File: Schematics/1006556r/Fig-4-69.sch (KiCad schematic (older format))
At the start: 0 parts

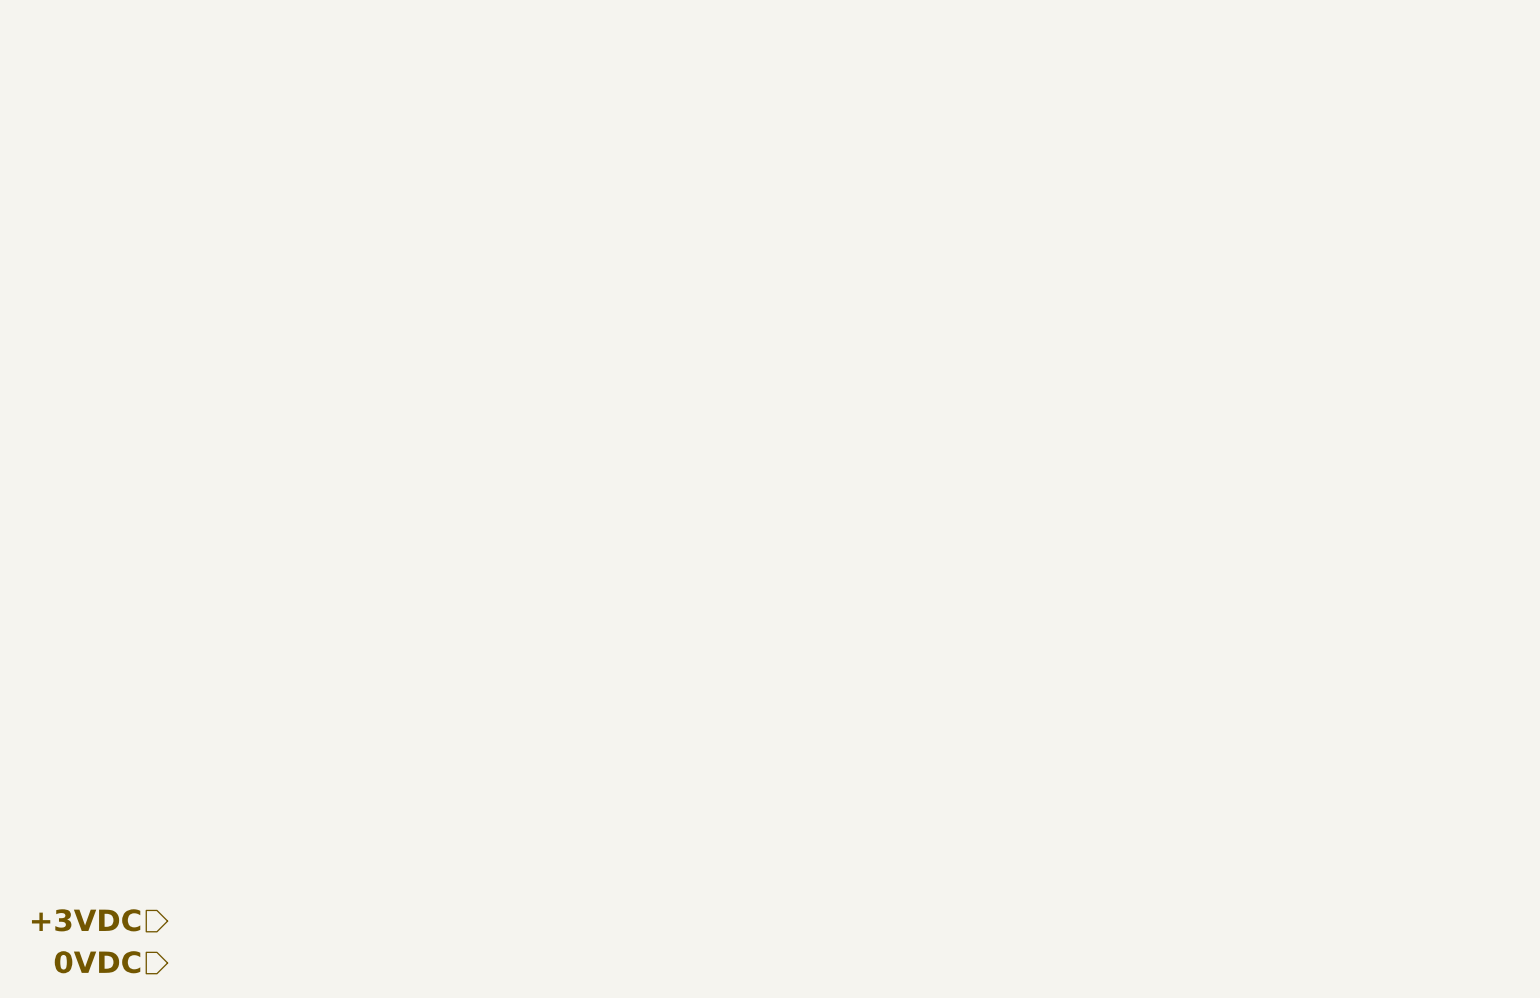
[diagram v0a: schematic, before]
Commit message: For module A31, transcribed through Fig 4-87, leaving just 88, 91, 93, 114, 141, and 147 to go, plus their integration into the top-level sheet (and resolution of remaining inconsistencies in ND-1021041).
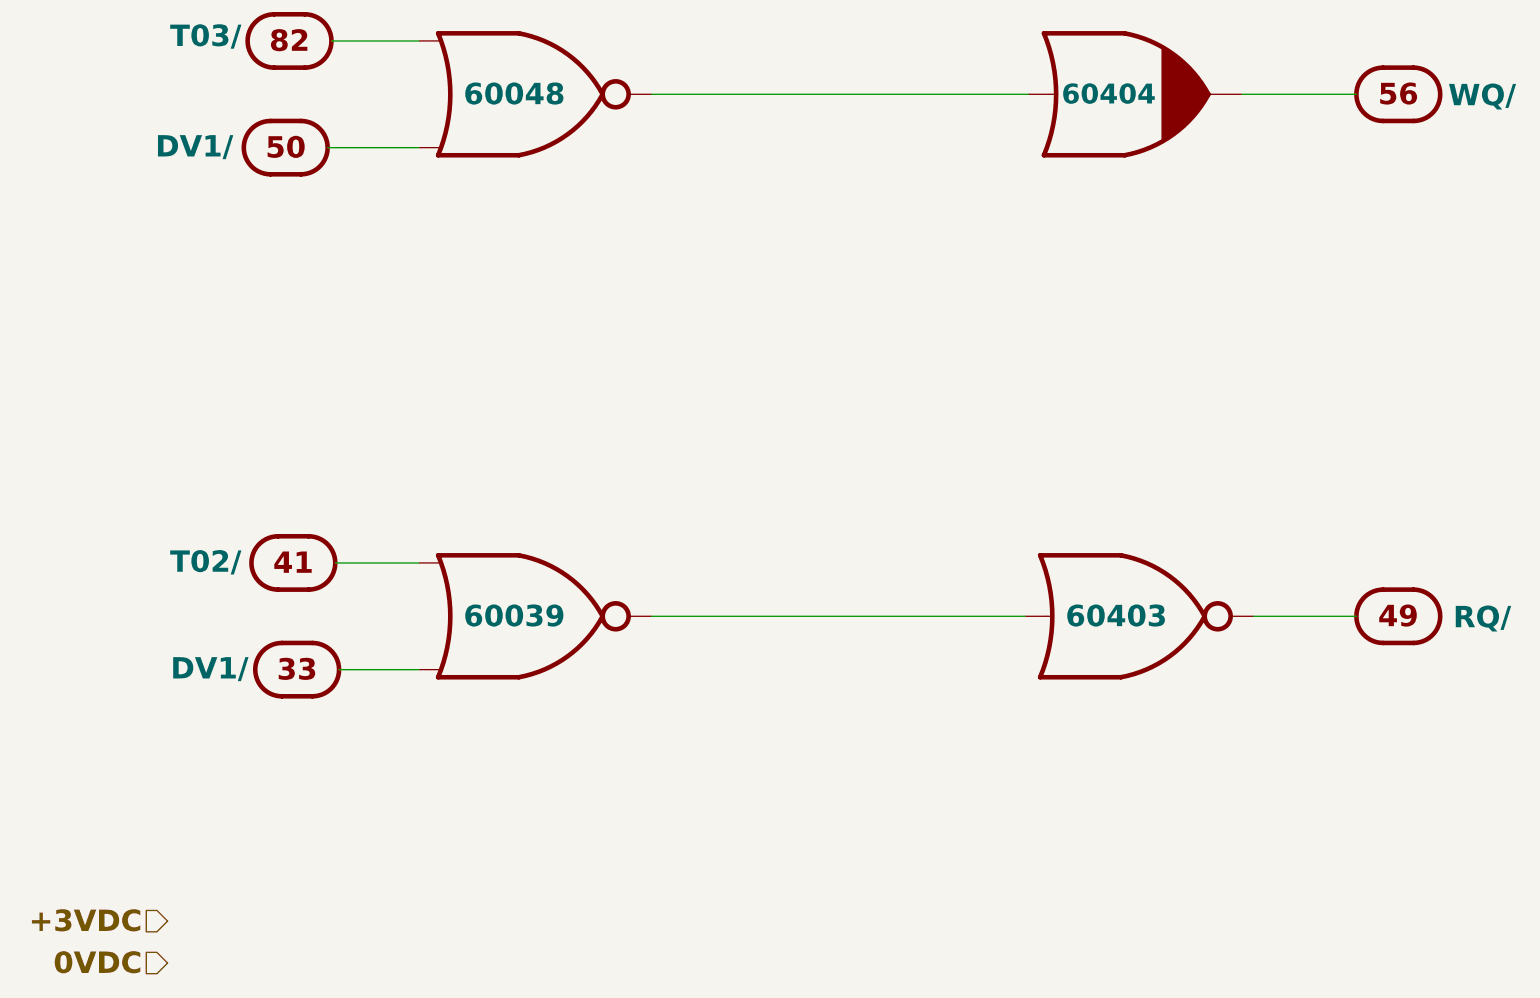
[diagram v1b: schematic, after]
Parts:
- added J1: ConnectorGeneric, symbol AGC_DSKY:ConnectorGeneric
- added U?: D3NOR-+3VDC-0VDC-nd1021041-_B_-___, symbol D3NOR-+3VDC-0VDC-nd1021041:D3NOR-+3VDC-0VDC-nd1021041-_B_-___
- added U? (x2): D3NOR-+3VDC-0VDC-nd1021041-A_C-___, symbol D3NOR-+3VDC-0VDC-nd1021041:D3NOR-+3VDC-0VDC-nd1021041-A_C-___
- added U?: D3NOR-NC-0VDC-expander-nd1021041-_B_-___, symbol D3NOR-NC-0VDC-expander-nd1021041:D3NOR-NC-0VDC-expander-nd1021041-_B_-___
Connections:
- net +3VDC: now also U?.6 (+3VDC), U?.6 (+3VDC), U?.6 (+3VDC)
- net 0VDC: now also U?.2 (0VDC), U?.2 (0VDC), U?.3 (0VDC), U?.3 (0VDC), U?.4 (0VDC), U?.4 (0VDC), U?.5 (0VDC), U?.5 (0VDC), U?.5 (0VDC), U?.5 (0VDC)
- new net: J1.82, U?.4 (A)
- new net: J1.49, U?.1 (J)
- new net: J1.41, U?.4 (A)
- new net: U?.1 (J), U?.3 (B) (x2)
- new net: J1.50, U?.2 (C)
- new net: J1.56, U?.1 (J)
- new net: J1.33, U?.2 (C)
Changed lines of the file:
@@
 Sheet 9 24
 Title "BLOCK I LOGIC FLOW S, MODULE A21, DRAWING 1006556"
-Date "2018-11-24"
+Date "2018-11-25"
 Rev "Draft"
 Comp ""
@@
 Text HLabel 1600 7475 0    140  Input ~ 28
 0VDC
+$Comp
+L AGC_DSKY:ConnectorGeneric J1
+U 82 1 5BF9D1BE
+P 2400 1425
+F 0 "J1" H 2400 1750 140 0001 C CNN
+F 1 "ConnectorGeneric" H 2400 1850 140 0001 C CNN
+F 2 "" H 2400 1900 140 0001 C CNN
+F 3 "" H 2400 1900 140 0001 C CNN
+F 4 "T03/" H 1850 1375 140 0000 C BNB "Caption"
+	82   2400 1425
+	1    0    0    -1
+$EndComp
+$Comp
+L AGC_DSKY:ConnectorGeneric J1
+U 49 1 5BF9D1BF
+P 9675 5200
+F 0 "J1" H 9675 5525 140 0001 C CNN
+F 1 "ConnectorGeneric" H 9675 5625 140 0001 C CNN
+F 2 "" H 9675 5675 140 0001 C CNN
+F 3 "" H 9675 5675 140 0001 C CNN
+F 4 "RQ/" H 9125 5125 140 0000 C BNB "Caption"
+	49   9675 5200
+	-1   0    0    1
+$EndComp
+$Comp
+L AGC_DSKY:ConnectorGeneric J1
+U 41 1 5BF9D1C0
+P 2425 4850
+F 0 "J1" H 2425 5175 140 0001 C CNN
+F 1 "ConnectorGeneric" H 2425 5275 140 0001 C CNN
+F 2 "" H 2425 5325 140 0001 C CNN
+F 3 "" H 2425 5325 140 0001 C CNN
+F 4 "T02/" H 1850 4775 140 0000 C BNB "Caption"
+	41   2425 4850
+	1    0    0    -1
+$EndComp
+$Comp
+L D3NOR-+3VDC-0VDC-nd1021041:D3NOR-+3VDC-0VDC-nd1021041-_B_-___ U?
+U 1 1 5BF9D1C1
+P 7825 5200
+F 0 "U?" H 7825 5525 140 0001 C CNB
+F 1 "D3NOR-+3VDC-0VDC-nd1021041-_B_-___" H 7825 5625 140 0001 C CNN
+F 2 "" H 7825 5675 140 0001 C CNN
+F 3 "" H 7825 5675 140 0001 C CNN
+F 4 "60403" H 7825 5200 140 0000 C CNB "Location"
+	1    7825 5200
+	1    0    0    1
+$EndComp
+$Comp
+L D3NOR-+3VDC-0VDC-nd1021041:D3NOR-+3VDC-0VDC-nd1021041-A_C-___ U?
+U 1 1 5BF9D1C2
+P 3875 1775
+F 0 "U?" H 3875 2100 140 0001 C CNB
+F 1 "D3NOR-+3VDC-0VDC-nd1021041-A_C-___" H 3875 2200 140 0001 C CNN
+F 2 "" H 3875 2250 140 0001 C CNN
+F 3 "" H 3875 2250 140 0001 C CNN
+F 4 "60048" H 3875 1775 140 0000 C CNB "Location"
+	1    3875 1775
+	1    0    0    -1
+$EndComp
+$Comp
+L AGC_DSKY:ConnectorGeneric J1
+U 50 1 5BF9D1C3
+P 2375 2125
+F 0 "J1" H 2375 2450 140 0001 C CNN
+F 1 "ConnectorGeneric" H 2375 2550 140 0001 C CNN
+F 2 "" H 2375 2600 140 0001 C CNN
+F 3 "" H 2375 2600 140 0001 C CNN
+F 4 "DV1/" H 1775 2050 140 0000 C BNB "Caption"
+	50   2375 2125
+	1    0    0    -1
+$EndComp
+$Comp
+L AGC_DSKY:ConnectorGeneric J1
+U 56 1 5BF9D1C4
+P 9675 1775
+F 0 "J1" H 9675 2100 140 0001 C CNN
+F 1 "ConnectorGeneric" H 9675 2200 140 0001 C CNN
+F 2 "" H 9675 2250 140 0001 C CNN
+F 3 "" H 9675 2250 140 0001 C CNN
+F 4 "WQ/" H 9125 1700 140 0000 C BNB "Caption"
+	56   9675 1775
+	-1   0    0    1
+$EndComp
+$Comp
+L D3NOR-NC-0VDC-expander-nd1021041:D3NOR-NC-0VDC-expander-nd1021041-_B_-___ U?
+U 1 1 5BF9D1C5
+P 7850 1775
+F 0 "U?" H 7850 2100 140 0001 C CNB
+F 1 "D3NOR-NC-0VDC-expander-nd1021041-_B_-___" H 7850 2200 140 0001 C CNN
+F 2 "" H 7850 2250 140 0001 C CNN
+F 3 "" H 7850 2250 140 0001 C CNN
+F 4 "60404" H 7775 1775 130 0000 C CNB "Location"
+	1    7850 1775
+	1    0    0    1
+$EndComp
+$Comp
+L AGC_DSKY:ConnectorGeneric J1
+U 33 1 5BF9D1C6
+P 2450 5550
+F 0 "J1" H 2450 5875 140 0001 C CNN
+F 1 "ConnectorGeneric" H 2450 5975 140 0001 C CNN
+F 2 "" H 2450 6025 140 0001 C CNN
+F 3 "" H 2450 6025 140 0001 C CNN
+F 4 "DV1/" H 1875 5475 140 0000 C BNB "Caption"
+	33   2450 5550
+	1    0    0    -1
+$EndComp
+$Comp
+L D3NOR-+3VDC-0VDC-nd1021041:D3NOR-+3VDC-0VDC-nd1021041-A_C-___ U?
+U 1 1 5BF9D1C7
+P 3875 5200
+F 0 "U?" H 3875 5525 140 0001 C CNB
+F 1 "D3NOR-+3VDC-0VDC-nd1021041-A_C-___" H 3875 5625 140 0001 C CNN
+F 2 "" H 3875 5675 140 0001 C CNN
+F 3 "" H 3875 5675 140 0001 C CNN
+F 4 "60039" H 3875 5200 140 0000 C CNB "Location"
+	1    3875 5200
+	1    0    0    -1
+$EndComp
+Wire Wire Line
+	4775 1775 7250 1775
+Wire Wire Line
+	7225 5200 4775 5200
+Wire Wire Line
+	3250 1425 2675 1425
+Wire Wire Line
+	3250 2125 2650 2125
+Wire Wire Line
+	8650 1775 9400 1775
+Wire Wire Line
+	8725 5200 9400 5200
+Wire Wire Line
+	3250 5550 2725 5550
+Wire Wire Line
+	3250 4850 2700 4850
 $EndSCHEMATC

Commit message: Finished up transcription of drawing 1006556 (Block I logic flow S, module A21).  But it may be a total mess, so user beware!
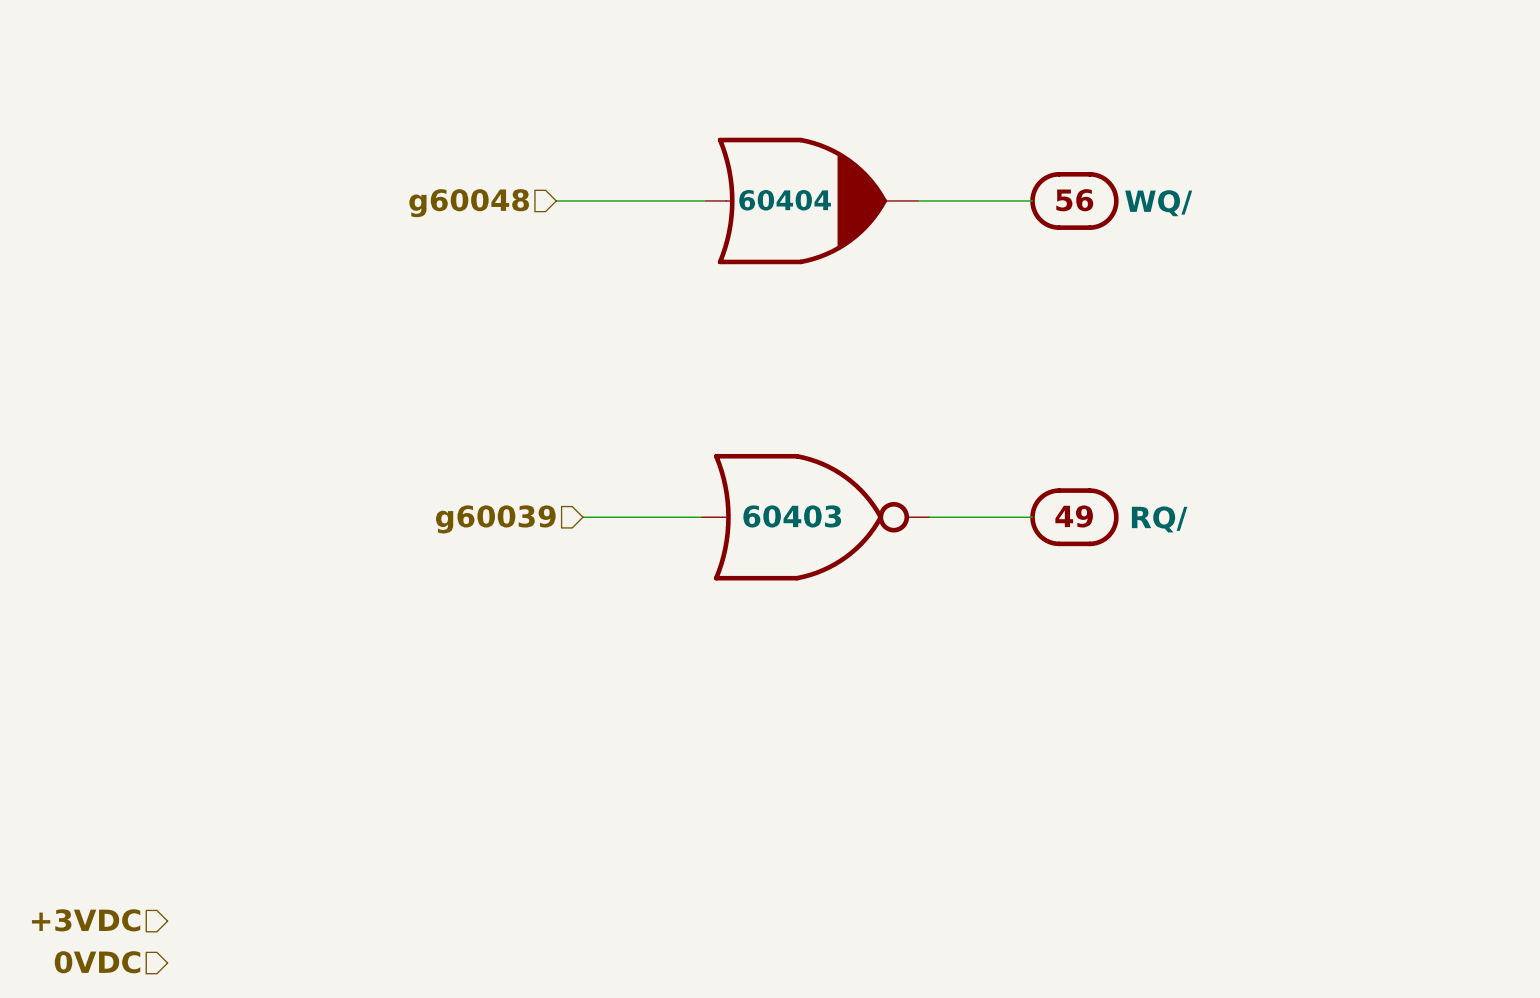
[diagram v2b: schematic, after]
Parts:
- removed unit 82 of J1
- removed unit 41 of J1
- removed unit 50 of J1
- removed unit 33 of J1
- removed U? (x2): D3NOR-+3VDC-0VDC-nd1021041-A_C-___, symbol D3NOR-+3VDC-0VDC-nd1021041:D3NOR-+3VDC-0VDC-nd1021041-A_C-___
- gave numbers to parts that had none: 2
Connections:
- net g60039: now reaches U901.3 (B)
- net g60048: now reaches U902.3 (B)
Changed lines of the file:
@@
-$Comp
-L AGC_DSKY:ConnectorGeneric J1
-U 82 1 5BF9D1BE
-P 2400 1425
-F 0 "J1" H 2400 1750 140 0001 C CNN
-F 1 "ConnectorGeneric" H 2400 1850 140 0001 C CNN
-F 2 "" H 2400 1900 140 0001 C CNN
-F 3 "" H 2400 1900 140 0001 C CNN
-F 4 "T03/" H 1850 1375 140 0000 C BNB "Caption"
-	82   2400 1425
-	1    0    0    -1
-$EndComp
 $Comp
 L AGC_DSKY:ConnectorGeneric J1
 U 49 1 5BF9D1BF
-P 9675 5200
-F 0 "J1" H 9675 5525 140 0001 C CNN
-F 1 "ConnectorGeneric" H 9675 5625 140 0001 C CNN
-F 2 "" H 9675 5675 140 0001 C CNN
-F 3 "" H 9675 5675 140 0001 C CNN
-F 4 "RQ/" H 9125 5125 140 0000 C BNB "Caption"
-	49   9675 5200
+P 7550 4550
+F 0 "J1" H 7550 4875 140 0001 C CNN
+F 1 "ConnectorGeneric" H 7550 4975 140 0001 C CNN
+F 2 "" H 7550 5025 140 0001 C CNN
+F 3 "" H 7550 5025 140 0001 C CNN
+F 4 "RQ/" H 7000 4475 140 0000 C BNB "Caption"
+	49   7550 4550
 	-1   0    0    1
 $EndComp
 $Comp
-L AGC_DSKY:ConnectorGeneric J1
-U 41 1 5BF9D1C0
-P 2425 4850
-F 0 "J1" H 2425 5175 140 0001 C CNN
-F 1 "ConnectorGeneric" H 2425 5275 140 0001 C CNN
-F 2 "" H 2425 5325 140 0001 C CNN
-F 3 "" H 2425 5325 140 0001 C CNN
-F 4 "T02/" H 1850 4775 140 0000 C BNB "Caption"
-	41   2425 4850
-	1    0    0    -1
-$EndComp
-$Comp
-L D3NOR-+3VDC-0VDC-nd1021041:D3NOR-+3VDC-0VDC-nd1021041-_B_-___ U?
+L D3NOR-+3VDC-0VDC-nd1021041:D3NOR-+3VDC-0VDC-nd1021041-_B_-___ U901
 U 1 1 5BF9D1C1
-P 7825 5200
-F 0 "U?" H 7825 5525 140 0001 C CNB
-F 1 "D3NOR-+3VDC-0VDC-nd1021041-_B_-___" H 7825 5625 140 0001 C CNN
-F 2 "" H 7825 5675 140 0001 C CNN
-F 3 "" H 7825 5675 140 0001 C CNN
-F 4 "60403" H 7825 5200 140 0000 C CNB "Location"
-	1    7825 5200
+P 5700 4550
+F 0 "U901" H 5700 4875 140 0001 C CNB
+F 1 "D3NOR-+3VDC-0VDC-nd1021041-_B_-___" H 5700 4975 140 0001 C CNN
+F 2 "" H 5700 5025 140 0001 C CNN
+F 3 "" H 5700 5025 140 0001 C CNN
+F 4 "60403" H 5700 4550 140 0000 C CNB "Location"
+	1    5700 4550
 	1    0    0    1
-$EndComp
-$Comp
-L D3NOR-+3VDC-0VDC-nd1021041:D3NOR-+3VDC-0VDC-nd1021041-A_C-___ U?
-U 1 1 5BF9D1C2
-P 3875 1775
-F 0 "U?" H 3875 2100 140 0001 C CNB
-F 1 "D3NOR-+3VDC-0VDC-nd1021041-A_C-___" H 3875 2200 140 0001 C CNN
-F 2 "" H 3875 2250 140 0001 C CNN
-F 3 "" H 3875 2250 140 0001 C CNN
-F 4 "60048" H 3875 1775 140 0000 C CNB "Location"
-	1    3875 1775
-	1    0    0    -1
-$EndComp
-$Comp
-L AGC_DSKY:ConnectorGeneric J1
-U 50 1 5BF9D1C3
-P 2375 2125
-F 0 "J1" H 2375 2450 140 0001 C CNN
-F 1 "ConnectorGeneric" H 2375 2550 140 0001 C CNN
-F 2 "" H 2375 2600 140 0001 C CNN
-F 3 "" H 2375 2600 140 0001 C CNN
-F 4 "DV1/" H 1775 2050 140 0000 C BNB "Caption"
-	50   2375 2125
-	1    0    0    -1
 $EndComp
 $Comp
 L AGC_DSKY:ConnectorGeneric J1
 U 56 1 5BF9D1C4
-P 9675 1775
-F 0 "J1" H 9675 2100 140 0001 C CNN
-F 1 "ConnectorGeneric" H 9675 2200 140 0001 C CNN
-F 2 "" H 9675 2250 140 0001 C CNN
-F 3 "" H 9675 2250 140 0001 C CNN
-F 4 "WQ/" H 9125 1700 140 0000 C BNB "Caption"
-	56   9675 1775
+P 7550 2475
+F 0 "J1" H 7550 2800 140 0001 C CNN
+F 1 "ConnectorGeneric" H 7550 2900 140 0001 C CNN
+F 2 "" H 7550 2950 140 0001 C CNN
+F 3 "" H 7550 2950 140 0001 C CNN
+F 4 "WQ/" H 7000 2400 140 0000 C BNB "Caption"
+	56   7550 2475
 	-1   0    0    1
 $EndComp
 $Comp
-L D3NOR-NC-0VDC-expander-nd1021041:D3NOR-NC-0VDC-expander-nd1021041-_B_-___ U?
+L D3NOR-NC-0VDC-expander-nd1021041:D3NOR-NC-0VDC-expander-nd1021041-_B_-___ U902
 U 1 1 5BF9D1C5
-P 7850 1775
-F 0 "U?" H 7850 2100 140 0001 C CNB
-F 1 "D3NOR-NC-0VDC-expander-nd1021041-_B_-___" H 7850 2200 140 0001 C CNN
-F 2 "" H 7850 2250 140 0001 C CNN
-F 3 "" H 7850 2250 140 0001 C CNN
-F 4 "60404" H 7775 1775 130 0000 C CNB "Location"
-	1    7850 1775
+P 5725 2475
+F 0 "U902" H 5725 2800 140 0001 C CNB
+F 1 "D3NOR-NC-0VDC-expander-nd1021041-_B_-___" H 5725 2900 140 0001 C CNN
+F 2 "" H 5725 2950 140 0001 C CNN
+F 3 "" H 5725 2950 140 0001 C CNN
+F 4 "60404" H 5650 2475 130 0000 C CNB "Location"
+	1    5725 2475
 	1    0    0    1
 $EndComp
-$Comp
-L AGC_DSKY:ConnectorGeneric J1
-U 33 1 5BF9D1C6
-P 2450 5550
-F 0 "J1" H 2450 5875 140 0001 C CNN
-F 1 "ConnectorGeneric" H 2450 5975 140 0001 C CNN
-F 2 "" H 2450 6025 140 0001 C CNN
-F 3 "" H 2450 6025 140 0001 C CNN
-F 4 "DV1/" H 1875 5475 140 0000 C BNB "Caption"
-	33   2450 5550
-	1    0    0    -1
-$EndComp
-$Comp
-L D3NOR-+3VDC-0VDC-nd1021041:D3NOR-+3VDC-0VDC-nd1021041-A_C-___ U?
-U 1 1 5BF9D1C7
-P 3875 5200
-F 0 "U?" H 3875 5525 140 0001 C CNB
-F 1 "D3NOR-+3VDC-0VDC-nd1021041-A_C-___" H 3875 5625 140 0001 C CNN
-F 2 "" H 3875 5675 140 0001 C CNN
-F 3 "" H 3875 5675 140 0001 C CNN
-F 4 "60039" H 3875 5200 140 0000 C CNB "Location"
-	1    3875 5200
-	1    0    0    -1
-$EndComp
 Wire Wire Line
-	4775 1775 7250 1775
+	4150 2475 5125 2475
 Wire Wire Line
-	7225 5200 4775 5200
+	5100 4550 4325 4550
 Wire Wire Line
-	3250 1425 2675 1425
+	6525 2475 7275 2475
 Wire Wire Line
-	3250 2125 2650 2125
-Wire Wire Line
-	8650 1775 9400 1775
-Wire Wire Line
-	8725 5200 9400 5200
-Wire Wire Line
-	3250 5550 2725 5550
-Wire Wire Line
-	3250 4850 2700 4850
+	6600 4550 7275 4550
+Text HLabel 4150 2475 0    140  Input ~ 28
+g60048
+Text HLabel 4325 4550 0    140  Input ~ 28
+g60039
 $EndSCHEMATC

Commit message: When I started recovering transcribed Block I schematics from document ND-1021041, there was no info available to me on the pinout of the NOR-gates they used, and it didn't occur to me that any might be forthcoming, so I chose a pinout arbitrarily.  It turns out that we now have the required info (SCD 1006771), and my arbitrary choices were wrong. I've therefore updated the NOR-library generator script, the relevant NOR libraries themselves, and all of the so-far-recovered Block I schematics using those gates.  It doesn't really matter in the cosmic sense, since the real Block I schematics have become available in the meantime, so that these recovered schematics are of less interest, but it will come in handy when I eventually want to do cross-checking.  I haven't checked these updated schematics in full detail, but I've spot-checked them, and run some ERCs and netlists, and it looks good to me.
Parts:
- U901: value D3NOR-+3VDC-0VDC-nd1021041-_B_-___ -> D3NOR-+3VDC-0VDC-nd1021041-_3_-___; symbol D3NOR-+3VDC-0VDC-nd1021041:D3NOR-+3VDC-0VDC-nd1021041-_B_-___ -> D3NOR-+3VDC-0VDC-nd1021041:D3NOR-+3VDC-0VDC-nd1021041-_3_-___
- U902: value D3NOR-NC-0VDC-expander-nd1021041-_B_-___ -> D3NOR-NC-0VDC-expander-nd1021041-_3_-___; symbol D3NOR-NC-0VDC-expander-nd1021041:D3NOR-NC-0VDC-expander-nd1021041-_B_-___ -> D3NOR-NC-0VDC-expander-nd1021041:D3NOR-NC-0VDC-expander-nd1021041-_3_-___
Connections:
- net +3VDC: now also U901.8 (+3VDC); no longer U901.6 (+3VDC)
- net 0VDC: now also U901.1 (0VDC), U902.1 (0VDC); no longer U901.2 (0VDC), U902.2 (0VDC)
- net at J1.49: now also U901.7; no longer U901.1 (J)
- net at J1.56: now also U902.7; no longer U902.1 (J)
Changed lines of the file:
@@
 $EndComp
 $Comp
-L D3NOR-+3VDC-0VDC-nd1021041:D3NOR-+3VDC-0VDC-nd1021041-_B_-___ U901
+L D3NOR-+3VDC-0VDC-nd1021041:D3NOR-+3VDC-0VDC-nd1021041-_3_-___ U901
 U 1 1 5BF9D1C1
 P 5700 4550
 F 0 "U901" H 5700 4875 140 0001 C CNB
-F 1 "D3NOR-+3VDC-0VDC-nd1021041-_B_-___" H 5700 4975 140 0001 C CNN
+F 1 "D3NOR-+3VDC-0VDC-nd1021041-_3_-___" H 5700 4975 140 0001 C CNN
 F 2 "" H 5700 5025 140 0001 C CNN
 F 3 "" H 5700 5025 140 0001 C CNN
@@
 $EndComp
 $Comp
-L D3NOR-NC-0VDC-expander-nd1021041:D3NOR-NC-0VDC-expander-nd1021041-_B_-___ U902
+L D3NOR-NC-0VDC-expander-nd1021041:D3NOR-NC-0VDC-expander-nd1021041-_3_-___ U902
 U 1 1 5BF9D1C5
 P 5725 2475
 F 0 "U902" H 5725 2800 140 0001 C CNB
-F 1 "D3NOR-NC-0VDC-expander-nd1021041-_B_-___" H 5725 2900 140 0001 C CNN
+F 1 "D3NOR-NC-0VDC-expander-nd1021041-_3_-___" H 5725 2900 140 0001 C CNN
 F 2 "" H 5725 2950 140 0001 C CNN
 F 3 "" H 5725 2950 140 0001 C CNN
